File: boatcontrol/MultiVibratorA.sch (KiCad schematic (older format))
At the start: 6 parts, among them IC401 CD74HCT221E

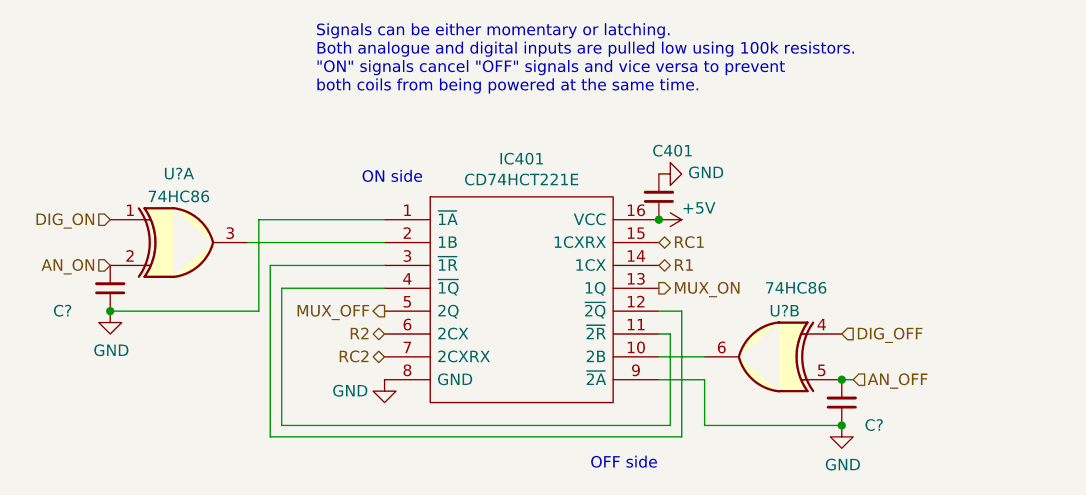
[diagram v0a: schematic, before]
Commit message: add second e-section
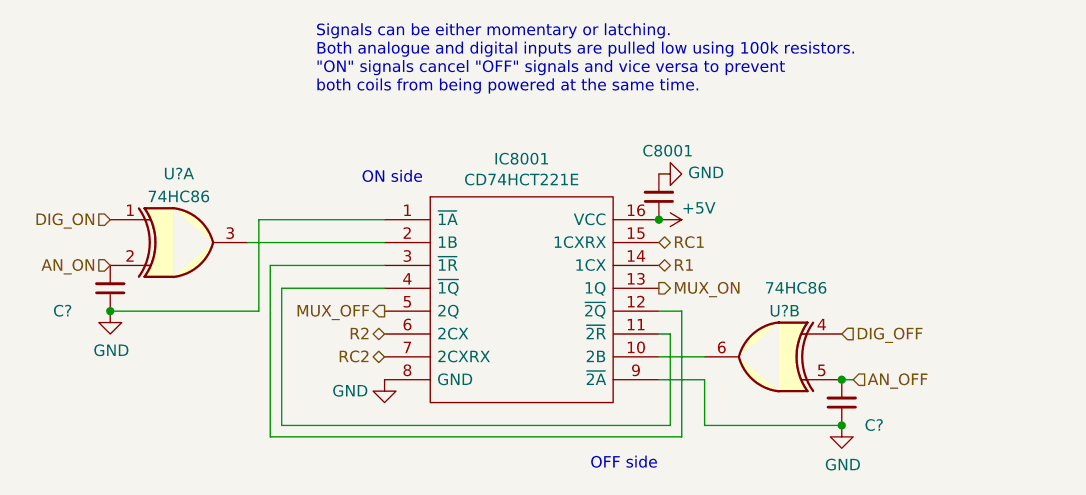
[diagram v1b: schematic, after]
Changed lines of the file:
@@
 $Descr A4 11693 8268
 encoding utf-8
-Sheet 10 97
+Sheet 68 97
 Title "Boat Control Hat"
 Date ""
@@
 AR Path="/D1BB8DB4/5F75E923/604747F3/603A29DF" Ref="IC7301"  Part="1"
 AR Path="/D1BB8DB4/5F75E923/604747FF/603A29DF" Ref="IC7401"  Part="1"
-F 0 "IC401" H 5450 4215 50  0000 C CNN
+F 0 "IC8001" H 5450 4215 50  0000 C CNN
 F 1 "CD74HCT221E" H 5450 4124 50  0000 C CNN
 F 2 "DIP794W53P254L1930H508Q16N" H 5900 4050 50  0001 L CNN
@@
 AR Path="/D1BB8DB4/5F75E923/604747F3/5FDA22CD" Ref="#PWR07302"  Part="1"
 AR Path="/D1BB8DB4/5F75E923/604747FF/5FDA22CD" Ref="#PWR07402"  Part="1"
-F 0 "#PWR0402" H 4850 4400 50  0001 C CNN
+F 0 "#PWR08002" H 4850 4400 50  0001 C CNN
 F 1 "GND" H 4700 4600 50  0000 C CNN
 F 2 "" H 4850 4650 50  0001 C CNN
@@
 AR Path="/D1BB8DB4/5F75E923/604747F3/603A29E0" Ref="#PWR07301"  Part="1"
 AR Path="/D1BB8DB4/5F75E923/604747FF/603A29E0" Ref="#PWR07401"  Part="1"
-F 0 "#PWR0401" H 6050 3800 50  0001 C CNN
+F 0 "#PWR08001" H 6050 3800 50  0001 C CNN
 F 1 "+5V" V 6000 4050 50  0000 L CNN
 F 2 "" H 6050 3950 50  0001 C CNN
@@
 AR Path="/D1BB8DB4/5F317CB5/60365B0F/603A29E9" Ref="#PWR0183"  Part="1"
 AR Path="/D1BB8DB4/5F317CB5/60365B35/603A29E9" Ref="#PWR0185"  Part="1"
-F 0 "#PWR0155" H 6050 3500 50  0001 C CNN
+F 0 "#PWR0183" H 6050 3500 50  0001 C CNN
 F 1 "GND" V 6055 3622 50  0000 R CNN
 F 2 "" H 6050 3750 50  0001 C CNN
@@
 AR Path="/D1BB8DB4/5F317CB5/60365B0F/603A29E8" Ref="C8001"  Part="1"
 AR Path="/D1BB8DB4/5F317CB5/60365B35/603A29E8" Ref="C8201"  Part="1"
-F 0 "C401" H 5900 3650 50  0000 L CNN
+F 0 "C8001" H 5900 3650 50  0000 L CNN
 F 1 "0.1μF" H 6141 3805 50  0001 L CNN
 F 2 "Capacitor_THT:C_Disc_D7.5mm_W5.0mm_P5.00mm" H 6050 3850 50  0001 C CNN
@@
 AR Path="/D16552B4/5FA17F38/61B95A95/602120C6" Ref="C?"  Part="1"
 AR Path="/D16552B4/5FA17F86/5FC6571E/602120C6" Ref="C?"  Part="1"
+AR Path="/D1BB8DB4/5F317CB5/60365B0F/602120C6" Ref="C?"  Part="1"
 F 0 "C?" H 6950 4850 50  0000 L CNN
 F 1 "1µF" H 6000 4650 50  0001 L CNN
@@
 AR Path="/D16552B4/5FA17F38/61B95A95/602124D8" Ref="#PWR?"  Part="1"
 AR Path="/D16552B4/5FA17F86/5FC6571E/602124D8" Ref="#PWR?"  Part="1"
+AR Path="/D1BB8DB4/5F317CB5/60365B0F/602124D8" Ref="#PWR?"  Part="1"
 F 0 "#PWR?" H 6850 4600 50  0001 C CNN
 F 1 "GND" H 6855 4677 50  0000 C CNN
@@
 AR Path="/D16552B4/5FA17F38/61B95A95/60416EE6" Ref="U?"  Part="1"
 AR Path="/D16552B4/5FA17F86/5FC6571E/60416EE6" Ref="U?"  Part="1"
+AR Path="/D1BB8DB4/5F317CB5/60365B0F/60416EE6" Ref="U?"  Part="1"
 F 0 "U?" H 3950 4350 50  0000 C CNN
 F 1 "74HC86" H 3950 4250 50  0000 C CNN
@@
 AR Path="/D16552B4/5FA17F38/61B95A95/603A29E5" Ref="#PWR?"  Part="1"
 AR Path="/D16552B4/5FA17F86/5FC6571E/603A29E5" Ref="#PWR?"  Part="1"
+AR Path="/D1BB8DB4/5F317CB5/60365B0F/603A29E5" Ref="#PWR?"  Part="1"
 F 0 "#PWR?" H 3650 4100 50  0001 C CNN
 F 1 "GND" H 3655 4177 50  0000 C CNN
@@
 AR Path="/D16552B4/5FA17F38/61B95A95/6021685A" Ref="C?"  Part="1"
 AR Path="/D16552B4/5FA17F86/5FC6571E/6021685A" Ref="C?"  Part="1"
+AR Path="/D1BB8DB4/5F317CB5/60365B0F/6021685A" Ref="C?"  Part="1"
 F 0 "C?" H 3400 4350 50  0000 L CNN
 F 1 "1µF" H 2800 4150 50  0001 L CNN
@@
 AR Path="/D16552B4/5FA17F38/61B95A95/60491845" Ref="U?"  Part="2"
 AR Path="/D16552B4/5FA17F86/5FC6571E/60491845" Ref="U?"  Part="2"
+AR Path="/D1BB8DB4/5F317CB5/60365B0F/60491845" Ref="U?"  Part="2"
 F 0 "U?" H 6500 4750 50  0000 C CNN
 F 1 "74HC86" H 6450 4850 50  0000 C CNN

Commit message: Top
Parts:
- removed C? (x2): 1µF, Capacitor_THT:C_Disc_D7.5mm_W5.0mm_P5.00mm, symbol Device:C_Small
- added C1001, C1002: 1µF, Capacitor_THT:C_Disc_D7.5mm_W5.0mm_P5.00mm, symbol Device:C_Small
- gave numbers to parts that had none: 1
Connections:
- net AN_OFF: now also C1002.2
- net AN_ON: now also C1001.2
- net GND: now also C1001.1, C1002.1

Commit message: Renamed
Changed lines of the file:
@@
 $Descr A4 11693 8268
 encoding utf-8
-Sheet 36 97
+Sheet 56 97
 Title "Boat Control Hat"
 Date ""
@@
 AR Path="/D1BB8DB4/5F75E923/604747F3/603A29DF" Ref="IC7301"  Part="1"
 AR Path="/D1BB8DB4/5F75E923/604747FF/603A29DF" Ref="IC7401"  Part="1"
-F 0 "IC3301" H 5450 4215 50  0000 C CNN
+F 0 "IC6401" H 5450 4215 50  0000 C CNN
 F 1 "CD74HCT221E" H 5450 4124 50  0000 C CNN
 F 2 "DIP794W53P254L1930H508Q16N" H 5900 4050 50  0001 L CNN
@@
 AR Path="/D1BB8DB4/5F75E923/604747F3/5FDA22CD" Ref="#PWR07302"  Part="1"
 AR Path="/D1BB8DB4/5F75E923/604747FF/5FDA22CD" Ref="#PWR07402"  Part="1"
-F 0 "#PWR03302" H 4850 4400 50  0001 C CNN
+F 0 "#PWR06402" H 4850 4400 50  0001 C CNN
 F 1 "GND" H 4700 4600 50  0000 C CNN
 F 2 "" H 4850 4650 50  0001 C CNN
@@
 AR Path="/D1BB8DB4/5F75E923/604747F3/603A29E0" Ref="#PWR07301"  Part="1"
 AR Path="/D1BB8DB4/5F75E923/604747FF/603A29E0" Ref="#PWR07401"  Part="1"
-F 0 "#PWR03301" H 6050 3800 50  0001 C CNN
+F 0 "#PWR06401" H 6050 3800 50  0001 C CNN
 F 1 "+5V" V 6000 4050 50  0000 L CNN
 F 2 "" H 6050 3950 50  0001 C CNN
@@
 AR Path="/D1BB8DB4/5F317CB5/60365B0F/603A29E9" Ref="#PWR0183"  Part="1"
 AR Path="/D1BB8DB4/5F317CB5/60365B35/603A29E9" Ref="#PWR0185"  Part="1"
-F 0 "#PWR0169" H 6050 3500 50  0001 C CNN
+F 0 "#PWR0177" H 6050 3500 50  0001 C CNN
 F 1 "GND" V 6055 3622 50  0000 R CNN
 F 2 "" H 6050 3750 50  0001 C CNN
@@
 AR Path="/D1BB8DB4/5F317CB5/60365B0F/603A29E8" Ref="C8001"  Part="1"
 AR Path="/D1BB8DB4/5F317CB5/60365B35/603A29E8" Ref="C8201"  Part="1"
-F 0 "C3301" H 5900 3650 50  0000 L CNN
+F 0 "C6401" H 5900 3650 50  0000 L CNN
 F 1 "0.1μF" H 6141 3805 50  0001 L CNN
 F 2 "Capacitor_THT:C_Disc_D7.5mm_W5.0mm_P5.00mm" H 6050 3850 50  0001 C CNN
@@
 AR Path="/D1BB8DB4/5F75E923/604747F3/60314A10" Ref="C6503"  Part="1"
 AR Path="/D1BB8DB4/5F317CB5/60365B35/60314A10" Ref="C7012"  Part="1"
-F 0 "C3602" H 6950 4850 50  0000 L CNN
+F 0 "C5603" H 6950 4850 50  0000 L CNN
 F 1 "1µF" H 6000 4650 50  0001 L CNN
 F 2 "Capacitor_THT:C_Disc_D7.5mm_W5.0mm_P5.00mm" H 6850 4750 50  0001 C CNN
@@
 AR Path="/D1BB8DB4/5F75E923/604747F3/602124D8" Ref="#PWR0337"  Part="1"
 AR Path="/D1BB8DB4/5F317CB5/60365B35/602124D8" Ref="#PWR0352"  Part="1"
-F 0 "#PWR0295" H 6850 4600 50  0001 C CNN
+F 0 "#PWR0326" H 6850 4600 50  0001 C CNN
 F 1 "GND" H 6855 4677 50  0000 C CNN
 F 2 "" H 6850 4850 50  0001 C CNN
@@
 AR Path="/D16552B4/5FA17F38/61B95A95/60416EE6" Ref="U?"  Part="1"
 AR Path="/D16552B4/5FA17F86/5FC6571E/60416EE6" Ref="U3002"  Part="1"
-AR Path="/D1BB8DB4/5F317CB5/60365B0F/60416EE6" Ref="U6801"  Part="1"
+AR Path="/D1BB8DB4/5F317CB5/60365B0F/60416EE6" Ref="U7902"  Part="1"
 AR Path="/D16552B4/5FA17F38/61B8E927/60416EE6" Ref="U303"  Part="1"
 AR Path="/D16552B4/5FA17F52/61B8E927/60416EE6" Ref="U1203"  Part="1"
@@
 AR Path="/D1BB8DB4/5F746103/60365B0F/60416EE6" Ref="U4002"  Part="1"
 AR Path="/D1BB8DB4/5F746103/60365B35/60416EE6" Ref="U4003"  Part="1"
-AR Path="/D1BB8DB4/5F76AF55/604747CD/60416EE6" Ref="U5001"  Part="1"
-AR Path="/D1BB8DB4/5F76AF55/604747F3/60416EE6" Ref="U5601"  Part="1"
-AR Path="/D1BB8DB4/5F75E923/604747CD/60416EE6" Ref="U5901"  Part="1"
-AR Path="/D1BB8DB4/5F75E923/604747F3/60416EE6" Ref="U6501"  Part="1"
-AR Path="/D1BB8DB4/5F317CB5/60365B35/60416EE6" Ref="U7002"  Part="1"
-F 0 "U3003" H 3950 4350 50  0000 C CNN
+AR Path="/D1BB8DB4/5F76AF55/604747CD/60416EE6" Ref="U6102"  Part="1"
+AR Path="/D1BB8DB4/5F76AF55/604747F3/60416EE6" Ref="U6103"  Part="1"
+AR Path="/D1BB8DB4/5F75E923/604747CD/60416EE6" Ref="U7002"  Part="1"
+AR Path="/D1BB8DB4/5F75E923/604747F3/60416EE6" Ref="U7003"  Part="1"
+AR Path="/D1BB8DB4/5F317CB5/60365B35/60416EE6" Ref="U7903"  Part="1"
+F 0 "U6103" H 3950 4350 50  0000 C CNN
 F 1 "74HC86" H 3950 4250 50  0000 C CNN
 F 2 "" H 3950 4050 50  0001 C CNN
@@
 AR Path="/D1BB8DB4/5F75E923/604747F3/603A29E5" Ref="#PWR0338"  Part="1"
 AR Path="/D1BB8DB4/5F317CB5/60365B35/603A29E5" Ref="#PWR0353"  Part="1"
-F 0 "#PWR0296" H 3650 4100 50  0001 C CNN
+F 0 "#PWR0327" H 3650 4100 50  0001 C CNN
 F 1 "GND" H 3655 4177 50  0000 C CNN
 F 2 "" H 3650 4350 50  0001 C CNN
@@
 AR Path="/D1BB8DB4/5F75E923/604747F3/60314A12" Ref="C6502"  Part="1"
 AR Path="/D1BB8DB4/5F317CB5/60365B35/60314A12" Ref="C7011"  Part="1"
-F 0 "C3601" H 3400 4350 50  0000 L CNN
+F 0 "C5602" H 3400 4350 50  0000 L CNN
 F 1 "1µF" H 2800 4150 50  0001 L CNN
 F 2 "Capacitor_THT:C_Disc_D7.5mm_W5.0mm_P5.00mm" H 3650 4250 50  0001 C CNN
@@
 AR Path="/D16552B4/5FA17F38/61B95A95/60491845" Ref="U?"  Part="2"
 AR Path="/D16552B4/5FA17F86/5FC6571E/60491845" Ref="U3002"  Part="2"
-AR Path="/D1BB8DB4/5F317CB5/60365B0F/60491845" Ref="U6801"  Part="2"
+AR Path="/D1BB8DB4/5F317CB5/60365B0F/60491845" Ref="U7902"  Part="2"
 AR Path="/D16552B4/5FA17F38/61B8E927/60491845" Ref="U303"  Part="2"
 AR Path="/D16552B4/5FA17F52/61B8E927/60491845" Ref="U1203"  Part="2"
@@
 AR Path="/D1BB8DB4/5F746103/60365B0F/60491845" Ref="U4002"  Part="2"
 AR Path="/D1BB8DB4/5F746103/60365B35/60491845" Ref="U4003"  Part="2"
-AR Path="/D1BB8DB4/5F76AF55/604747CD/60491845" Ref="U5001"  Part="2"
-AR Path="/D1BB8DB4/5F76AF55/604747F3/60491845" Ref="U5601"  Part="2"
-AR Path="/D1BB8DB4/5F75E923/604747CD/60491845" Ref="U5901"  Part="2"
-AR Path="/D1BB8DB4/5F75E923/604747F3/60491845" Ref="U6501"  Part="2"
-AR Path="/D1BB8DB4/5F317CB5/60365B35/60491845" Ref="U7002"  Part="2"
-F 0 "U3003" H 6500 4750 50  0000 C CNN
-F 1 "74HC86" H 6450 4850 50  0000 C CNN
+AR Path="/D1BB8DB4/5F76AF55/604747CD/60491845" Ref="U6102"  Part="2"
+AR Path="/D1BB8DB4/5F76AF55/604747F3/60491845" Ref="U6103"  Part="2"
+AR Path="/D1BB8DB4/5F75E923/604747CD/60491845" Ref="U7002"  Part="2"
+AR Path="/D1BB8DB4/5F75E923/604747F3/60491845" Ref="U7003"  Part="2"
+AR Path="/D1BB8DB4/5F317CB5/60365B35/60491845" Ref="U7903"  Part="2"
+F 0 "U6103" H 6500 4750 50  0000 C CNN
+F 1 "74HC86" H 6500 4850 50  0000 C CNN
 F 2 "" H 6550 4550 50  0001 C CNN
 F 3 "http://www.ti.com/lit/gpn/sn74HC86" H 6550 4550 50  0001 C CNN

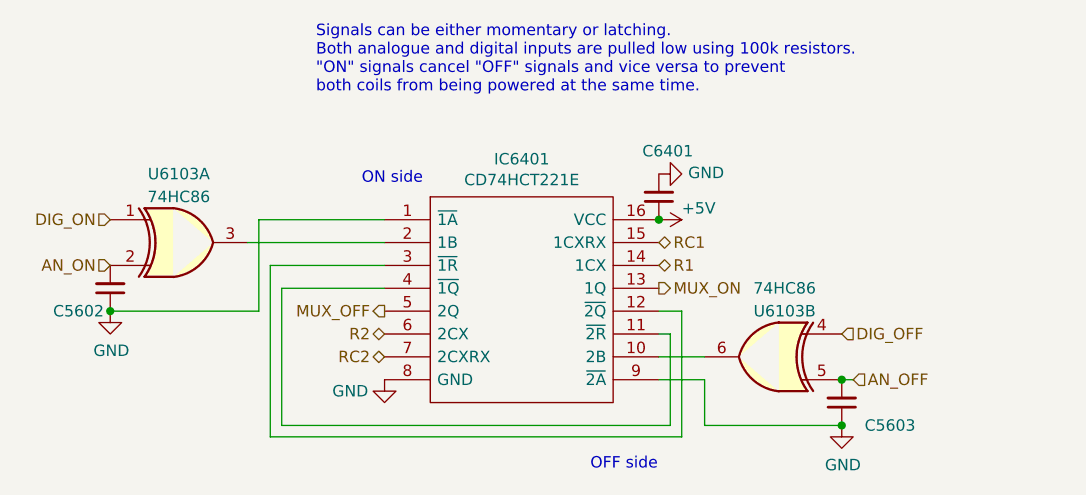
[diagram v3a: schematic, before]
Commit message: Update cap numbering
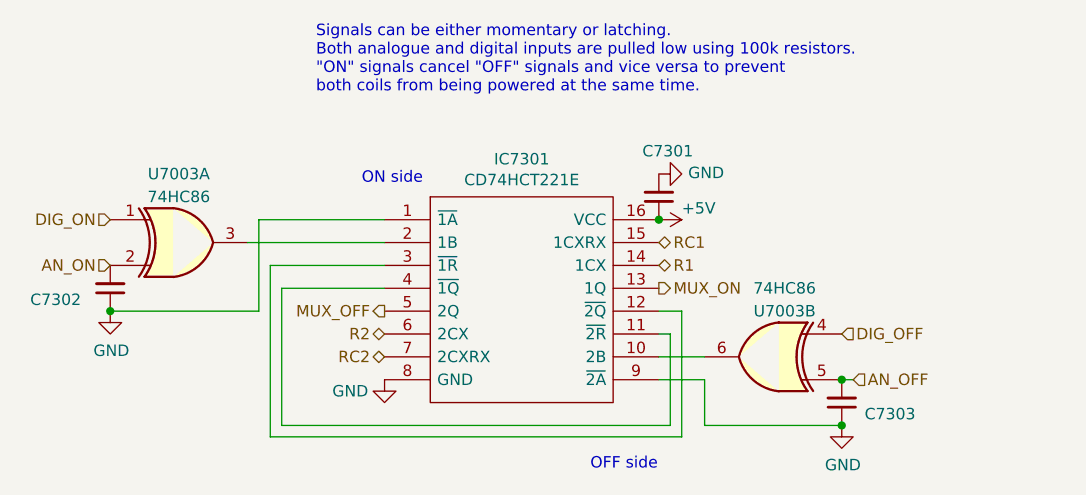
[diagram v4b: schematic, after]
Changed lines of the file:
@@
 $Descr A4 11693 8268
 encoding utf-8
-Sheet 56 97
+Sheet 65 97
 Title "Boat Control Hat"
 Date ""
@@
 AR Path="/D1BB8DB4/5F75E923/604747F3/603A29DF" Ref="IC7301"  Part="1"
 AR Path="/D1BB8DB4/5F75E923/604747FF/603A29DF" Ref="IC7401"  Part="1"
-F 0 "IC6401" H 5450 4215 50  0000 C CNN
+F 0 "IC7301" H 5450 4215 50  0000 C CNN
 F 1 "CD74HCT221E" H 5450 4124 50  0000 C CNN
 F 2 "DIP794W53P254L1930H508Q16N" H 5900 4050 50  0001 L CNN
@@
 AR Path="/D1BB8DB4/5F75E923/604747F3/5FDA22CD" Ref="#PWR07302"  Part="1"
 AR Path="/D1BB8DB4/5F75E923/604747FF/5FDA22CD" Ref="#PWR07402"  Part="1"
-F 0 "#PWR06402" H 4850 4400 50  0001 C CNN
+F 0 "#PWR07302" H 4850 4400 50  0001 C CNN
 F 1 "GND" H 4700 4600 50  0000 C CNN
 F 2 "" H 4850 4650 50  0001 C CNN
@@
 AR Path="/D1BB8DB4/5F75E923/604747F3/603A29E0" Ref="#PWR07301"  Part="1"
 AR Path="/D1BB8DB4/5F75E923/604747FF/603A29E0" Ref="#PWR07401"  Part="1"
-F 0 "#PWR06401" H 6050 3800 50  0001 C CNN
+F 0 "#PWR07301" H 6050 3800 50  0001 C CNN
 F 1 "+5V" V 6000 4050 50  0000 L CNN
 F 2 "" H 6050 3950 50  0001 C CNN
@@
 AR Path="/D1BB8DB4/5F317CB5/60365B0F/603A29E9" Ref="#PWR0183"  Part="1"
 AR Path="/D1BB8DB4/5F317CB5/60365B35/603A29E9" Ref="#PWR0185"  Part="1"
-F 0 "#PWR0177" H 6050 3500 50  0001 C CNN
+F 0 "#PWR0181" H 6050 3500 50  0001 C CNN
 F 1 "GND" V 6055 3622 50  0000 R CNN
 F 2 "" H 6050 3750 50  0001 C CNN
@@
 AR Path="/D1BB8DB4/5F317CB5/60365B0F/603A29E8" Ref="C8001"  Part="1"
 AR Path="/D1BB8DB4/5F317CB5/60365B35/603A29E8" Ref="C8201"  Part="1"
-F 0 "C6401" H 5900 3650 50  0000 L CNN
+F 0 "C7301" H 5900 3650 50  0000 L CNN
 F 1 "0.1μF" H 6141 3805 50  0001 L CNN
 F 2 "Capacitor_THT:C_Disc_D7.5mm_W5.0mm_P5.00mm" H 6050 3850 50  0001 C CNN
@@
 AR Path="/D16552B4/5FA17F38/61B95A95/60314A10" Ref="C?"  Part="1"
 AR Path="/D16552B4/5FA17F86/5FC6571E/60314A10" Ref="C3702"  Part="1"
-AR Path="/D1BB8DB4/5F317CB5/60365B0F/60314A10" Ref="C6802"  Part="1"
+AR Path="/D1BB8DB4/5F317CB5/60365B0F/60314A10" Ref="C8003"  Part="1"
 AR Path="/D16552B4/5FA17F38/61B8E927/60314A10" Ref="C902"  Part="1"
 AR Path="/D16552B4/5FA17F52/61B8E927/60314A10" Ref="C1802"  Part="1"
@@
 AR Path="/D16552B4/5FA17F6C/5FC6571E/60314A10" Ref="C2802"  Part="1"
 AR Path="/D16552B4/5FA17F86/61B8E927/60314A10" Ref="C3602"  Part="1"
-AR Path="/D1BB8DB4/5F746103/60365B0F/60314A10" Ref="C4102"  Part="1"
-AR Path="/D1BB8DB4/5F746103/60365B35/60314A10" Ref="C4302"  Part="1"
-AR Path="/D1BB8DB4/5F76AF55/604747CD/60314A10" Ref="C5002"  Part="1"
-AR Path="/D1BB8DB4/5F76AF55/604747F3/60314A10" Ref="C5603"  Part="1"
-AR Path="/D1BB8DB4/5F75E923/604747CD/60314A10" Ref="C5902"  Part="1"
-AR Path="/D1BB8DB4/5F75E923/604747F3/60314A10" Ref="C6503"  Part="1"
-AR Path="/D1BB8DB4/5F317CB5/60365B35/60314A10" Ref="C7012"  Part="1"
-F 0 "C5603" H 6950 4850 50  0000 L CNN
+AR Path="/D1BB8DB4/5F746103/60365B0F/60314A10" Ref="C5303"  Part="1"
+AR Path="/D1BB8DB4/5F746103/60365B35/60314A10" Ref="C5503"  Part="1"
+AR Path="/D1BB8DB4/5F76AF55/604747CD/60314A10" Ref="C6203"  Part="1"
+AR Path="/D1BB8DB4/5F76AF55/604747F3/60314A10" Ref="C6403"  Part="1"
+AR Path="/D1BB8DB4/5F75E923/604747CD/60314A10" Ref="C7103"  Part="1"
+AR Path="/D1BB8DB4/5F75E923/604747F3/60314A10" Ref="C7303"  Part="1"
+AR Path="/D1BB8DB4/5F317CB5/60365B35/60314A10" Ref="C8203"  Part="1"
+F 0 "C7303" H 6950 4800 50  0000 L CNN
 F 1 "1µF" H 6000 4650 50  0001 L CNN
 F 2 "Capacitor_THT:C_Disc_D7.5mm_W5.0mm_P5.00mm" H 6850 4750 50  0001 C CNN
@@
 AR Path="/D1BB8DB4/5F75E923/604747F3/602124D8" Ref="#PWR0337"  Part="1"
 AR Path="/D1BB8DB4/5F317CB5/60365B35/602124D8" Ref="#PWR0352"  Part="1"
-F 0 "#PWR0326" H 6850 4600 50  0001 C CNN
+F 0 "#PWR0337" H 6850 4600 50  0001 C CNN
 F 1 "GND" H 6855 4677 50  0000 C CNN
 F 2 "" H 6850 4850 50  0001 C CNN
@@
 AR Path="/D1BB8DB4/5F75E923/604747F3/60416EE6" Ref="U7003"  Part="1"
 AR Path="/D1BB8DB4/5F317CB5/60365B35/60416EE6" Ref="U7903"  Part="1"
-F 0 "U6103" H 3950 4350 50  0000 C CNN
+F 0 "U7003" H 3950 4350 50  0000 C CNN
 F 1 "74HC86" H 3950 4250 50  0000 C CNN
 F 2 "" H 3950 4050 50  0001 C CNN
@@
 AR Path="/D1BB8DB4/5F75E923/604747F3/603A29E5" Ref="#PWR0338"  Part="1"
 AR Path="/D1BB8DB4/5F317CB5/60365B35/603A29E5" Ref="#PWR0353"  Part="1"
-F 0 "#PWR0327" H 3650 4100 50  0001 C CNN
+F 0 "#PWR0338" H 3650 4100 50  0001 C CNN
 F 1 "GND" H 3655 4177 50  0000 C CNN
 F 2 "" H 3650 4350 50  0001 C CNN
@@
 AR Path="/D16552B4/5FA17F38/61B95A95/60314A12" Ref="C?"  Part="1"
 AR Path="/D16552B4/5FA17F86/5FC6571E/60314A12" Ref="C3701"  Part="1"
-AR Path="/D1BB8DB4/5F317CB5/60365B0F/60314A12" Ref="C6801"  Part="1"
+AR Path="/D1BB8DB4/5F317CB5/60365B0F/60314A12" Ref="C8002"  Part="1"
 AR Path="/D16552B4/5FA17F38/61B8E927/60314A12" Ref="C901"  Part="1"
 AR Path="/D16552B4/5FA17F52/61B8E927/60314A12" Ref="C1801"  Part="1"
@@
 AR Path="/D16552B4/5FA17F6C/5FC6571E/60314A12" Ref="C2801"  Part="1"
 AR Path="/D16552B4/5FA17F86/61B8E927/60314A12" Ref="C3601"  Part="1"
-AR Path="/D1BB8DB4/5F746103/60365B0F/60314A12" Ref="C4101"  Part="1"
-AR Path="/D1BB8DB4/5F746103/60365B35/60314A12" Ref="C4301"  Part="1"
-AR Path="/D1BB8DB4/5F76AF55/604747CD/60314A12" Ref="C5001"  Part="1"
-AR Path="/D1BB8DB4/5F76AF55/604747F3/60314A12" Ref="C5602"  Part="1"
-AR Path="/D1BB8DB4/5F75E923/604747CD/60314A12" Ref="C5901"  Part="1"
-AR Path="/D1BB8DB4/5F75E923/604747F3/60314A12" Ref="C6502"  Part="1"
-AR Path="/D1BB8DB4/5F317CB5/60365B35/60314A12" Ref="C7011"  Part="1"
-F 0 "C5602" H 3400 4350 50  0000 L CNN
+AR Path="/D1BB8DB4/5F746103/60365B0F/60314A12" Ref="C5302"  Part="1"
+AR Path="/D1BB8DB4/5F746103/60365B35/60314A12" Ref="C5502"  Part="1"
+AR Path="/D1BB8DB4/5F76AF55/604747CD/60314A12" Ref="C6202"  Part="1"
+AR Path="/D1BB8DB4/5F76AF55/604747F3/60314A12" Ref="C6402"  Part="1"
+AR Path="/D1BB8DB4/5F75E923/604747CD/60314A12" Ref="C7102"  Part="1"
+AR Path="/D1BB8DB4/5F75E923/604747F3/60314A12" Ref="C7302"  Part="1"
+AR Path="/D1BB8DB4/5F317CB5/60365B35/60314A12" Ref="C8202"  Part="1"
+F 0 "C7302" H 3300 4300 50  0000 L CNN
 F 1 "1µF" H 2800 4150 50  0001 L CNN
 F 2 "Capacitor_THT:C_Disc_D7.5mm_W5.0mm_P5.00mm" H 3650 4250 50  0001 C CNN
@@
 AR Path="/D1BB8DB4/5F75E923/604747F3/60491845" Ref="U7003"  Part="2"
 AR Path="/D1BB8DB4/5F317CB5/60365B35/60491845" Ref="U7903"  Part="2"
-F 0 "U6103" H 6500 4750 50  0000 C CNN
+F 0 "U7003" H 6500 4750 50  0000 C CNN
 F 1 "74HC86" H 6500 4850 50  0000 C CNN
 F 2 "" H 6550 4550 50  0001 C CNN
